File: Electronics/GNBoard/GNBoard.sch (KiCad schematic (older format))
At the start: 48 parts, among them K1 IR1, K10 IR4, K11 CNY_1, K12 CNY_2, K13 CNY_3, K14 CNY_4, K15 CNY_5, K16 CNY_6, K2 IR2, K3 SERVO_1, K4 SERVO_2, K5 SERVO_3, K6 SERVO_4, K7 SERVO_5, K8 SERVO_6, K9 IR3, P1 Battery, P2 CONN_5, P3 Spk, P4 I2C_1, P5 I2C_2, P6 DHT_Conn, SW1 PowerSwitch, SW2 SW_PUSH, SW3 SW_PUSH, U1 LM2576

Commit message: Finished first version, added schematics
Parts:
- removed C6: 100uF, symbol CP1
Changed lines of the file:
@@
-EESchema Schematic File Version 2  date jue 13 jun 2013 11:23:18 CEST
+EESchema Schematic File Version 2  date jue 13 jun 2013 11:29:49 CEST
 LIBS:LED_RGB
 LIBS:vreg
@@
 Wire Notes Line
 	6550 3550 6550 4700
-Wire Wire Line
-	6450 4600 6450 4550
-Wire Wire Line
-	6450 4550 6300 4550
-$Comp
-L GND #PWR044
-U 1 1 51B992FE
-P 6450 4600
-F 0 "#PWR044" H 6450 4600 30  0001 C CNN
-F 1 "GND" H 6450 4530 30  0001 C CNN
-F 2 "" H 6450 4600 60  0000 C CNN
-F 3 "" H 6450 4600 60  0000 C CNN
-	1    6450 4600
-	1    0    0    -1
-$EndComp
-$Comp
-L +5V #PWR045
-U 1 1 51B992F8
-P 5800 4550
-F 0 "#PWR045" H 5800 4640 20  0001 C CNN
-F 1 "+5V" H 5800 4640 30  0000 C CNN
-F 2 "" H 5800 4550 60  0000 C CNN
-F 3 "" H 5800 4550 60  0000 C CNN
-	1    5800 4550
-	1    0    0    -1
-$EndComp
-Wire Wire Line
-	5900 4550 5800 4550
-$Comp
-L CP1 C6
-U 1 1 51B992F2
-P 6100 4550
-F 0 "C6" V 6150 4650 50  0000 L CNN
-F 1 "100uF" V 6150 4250 50  0000 L CNN
-F 2 "" H 6100 4550 60  0001 C CNN
-F 3 "" H 6100 4550 60  0001 C CNN
-	1    6100 4550
-	0    -1   -1   0
-$EndComp
 $EndSCHEMATC

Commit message: First tests, added source code
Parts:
- C2: value 100uF -> 1000uF
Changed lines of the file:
@@
-EESchema Schematic File Version 2  date jue 13 jun 2013 11:29:49 CEST
+EESchema Schematic File Version 2  date jue 13 jun 2013 23:11:20 CEST
 LIBS:LED_RGB
 LIBS:vreg
@@
 P 3950 2750
 F 0 "C2" H 4000 2850 50  0000 L CNN
-F 1 "100uF" H 4000 2650 50  0000 L CNN
+F 1 "1000uF" H 4000 2650 50  0000 L CNN
 F 2 "" H 3950 2750 60  0001 C CNN
 F 3 "" H 3950 2750 60  0001 C CNN

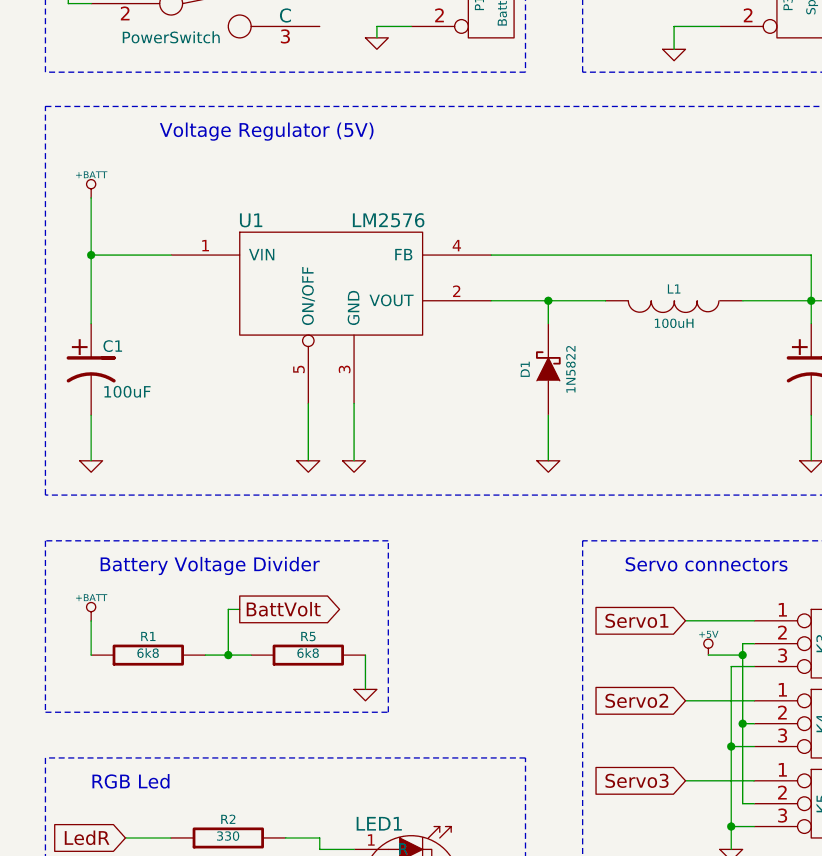
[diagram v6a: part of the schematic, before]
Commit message: Updated components to allow powering with up to 20V
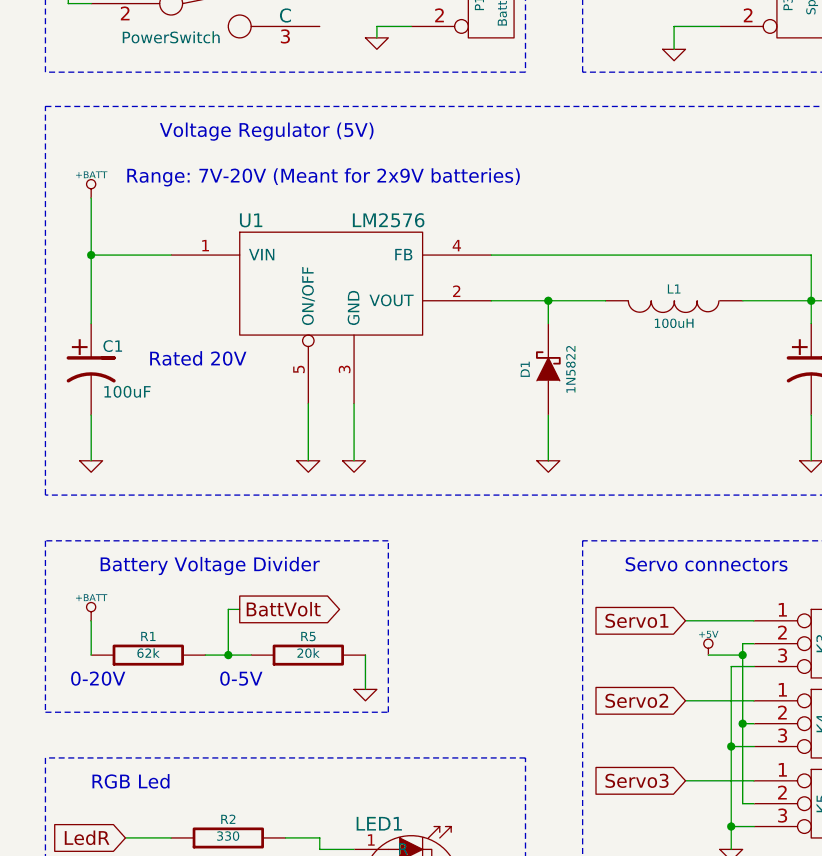
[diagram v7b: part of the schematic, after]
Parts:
- R1: value 6k8 -> 62k
- R5: value 6k8 -> 20k
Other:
- note added: "0-20V"
- note added: "0-5V"
- note added: "Range: 7V-20V (Meant for 2x9V batteries)"
- note added: "Rated 20V"
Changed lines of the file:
@@
-EESchema Schematic File Version 2  date jue 13 jun 2013 23:11:20 CEST
+EESchema Schematic File Version 2
 LIBS:LED_RGB
 LIBS:vreg
@@
 LIBS:valves
 LIBS:GNBoard-cache
-EELAYER 24 0
+EELAYER 27 0
 EELAYER END
 $Descr A4 11693 8268
@@
 Sheet 1 1
 Title ""
-Date "13 jun 2013"
+Date "14 jan 2014"
 Rev ""
 Comp ""
@@
 P 1050 4000
 F 0 "R1" V 1130 4000 40  0000 C CNN
-F 1 "6k8" V 1057 4001 40  0000 C CNN
+F 1 "62k" V 1057 4001 40  0000 C CNN
 F 2 "~" V 980 4000 30  0000 C CNN
 F 3 "~" H 1050 4000 30  0000 C CNN
@@
 P 1750 4000
 F 0 "R5" V 1830 4000 40  0000 C CNN
-F 1 "6k8" V 1757 4001 40  0000 C CNN
+F 1 "20k" V 1757 4001 40  0000 C CNN
 F 2 "~" V 1680 4000 30  0000 C CNN
 F 3 "~" H 1750 4000 30  0000 C CNN
@@
 Wire Notes Line
 	6550 3550 6550 4700
+Text Notes 950  1950 0    60   ~ 0
+Range: 7V-20V (Meant for 2x9V batteries)
+Text Notes 1050 2750 0    60   ~ 0
+Rated 20V
+Text Notes 1550 4150 2    60   ~ 0
+0-5V
+Text Notes 950  4150 2    60   ~ 0
+0-20V
 $EndSCHEMATC

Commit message: Working in new version for the GNBoard
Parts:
- removed K15: CNY_5, ~, symbol CONN_3
- removed K16: CNY_6, ~, symbol CONN_3
- removed P5: I2C_2, ~, symbol CONN_4
- added K17: Nose, ~, symbol CONN_3
- added M1: XBEE, xbee_r1-XBEE, symbol XBEE
- added R13, R14: 10k, ~, symbol R
- added R15, R16: 4k7, ~, symbol R
- added R17: 7k5, ~, symbol R
- added R18: 99k, ~, symbol R
- L1: Rated (none) -> 3A
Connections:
- net +5V: now also R14.1; no longer C5.1, SHIELD1.5V_4, SHIELD1.5V_5
- net GND: now also K17.2 (PM), M1.10 (GND@10), R17.1, R18.2; no longer P3.2 (PM), SHIELD1.GND4, SHIELD1.GND5
- net +3.3V: now reaches SHIELD1.3V3
- net +3.3V: now also C5.1, M1.1 (VCC@1)
- net Nose_V: now reaches SHIELD1.AD10
- net Nose_V: now also K17.1 (P1), R14.2
- net CNY5 renamed XB_DIN
- net XB_DIN: now also R16.1
- net CNY6 renamed XB_DOUT
- net XB_DOUT: now also R15.1
- new net: P3.2 (PM), R18.1
- new net: K17.3 (P3), R13.2
- new net: M1.2 (DOUT), R15.2
- new net: M1.3 (DIN), R16.2, R17.2
- new net Nose_heat: R13.1
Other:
- note added: "Electronic nose"
- note added: "XBEE wireless interface"
- moved on the sheet: C5, P3
